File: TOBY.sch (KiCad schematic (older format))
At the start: 36 parts, among them Q301 2N7002BKT, U301 U-BLOX-TOBY-L2, X301 ANT, X302 SIMcard, X303 ANT

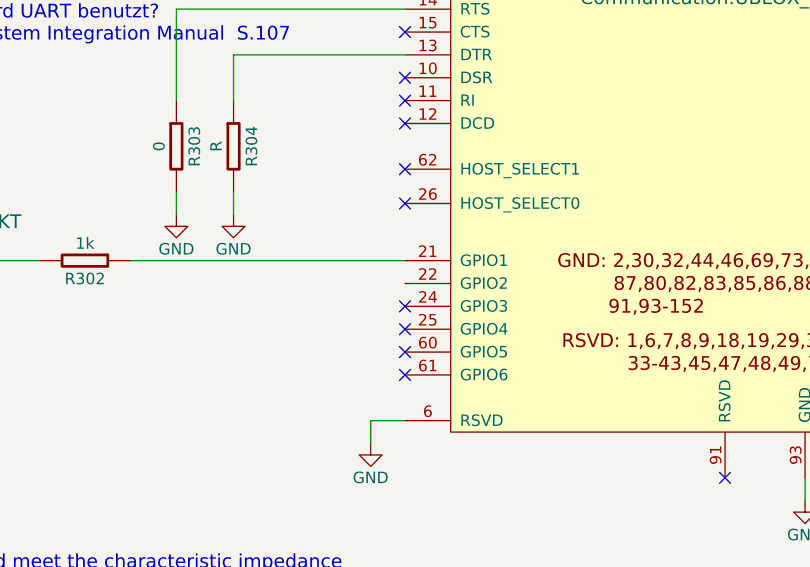
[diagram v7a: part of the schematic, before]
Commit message: adjusted 3d models
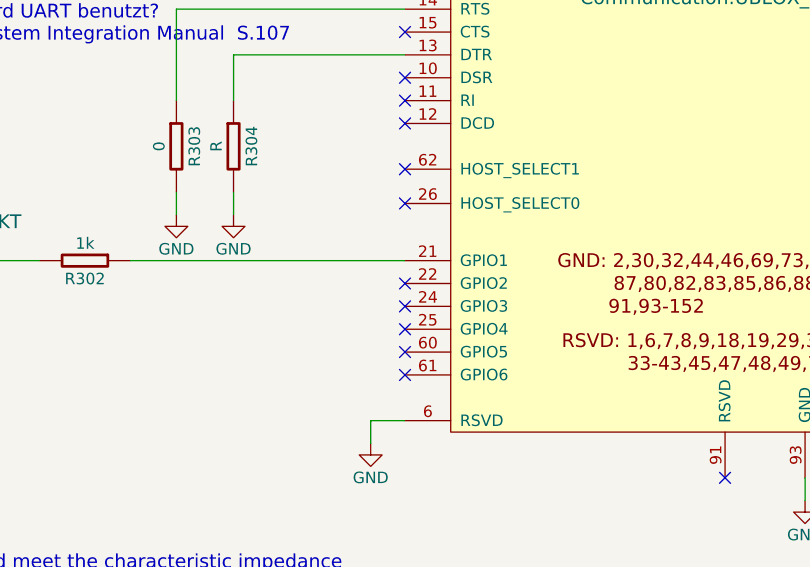
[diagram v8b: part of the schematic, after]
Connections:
- no-connect marks 26 -> 27
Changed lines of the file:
@@
 $EndComp
 $Comp
-L GND #PWR321
+L GND #PWR084
 U 1 1 570E3CB9
 P 9100 2450
-F 0 "#PWR321" H 9100 2200 50  0001 C CNN
+F 0 "#PWR084" H 9100 2200 50  0001 C CNN
 F 1 "GND" H 9100 2300 50  0000 C CNN
 F 2 "" H 9100 2450 50  0000 C CNN
@@
 $EndComp
 $Comp
-L GND #PWR322
+L GND #PWR085
 U 1 1 570E6A84
 P 10000 5500
-F 0 "#PWR322" H 10000 5250 50  0001 C CNN
+F 0 "#PWR085" H 10000 5250 50  0001 C CNN
 F 1 "GND" H 10000 5350 50  0000 C CNN
 F 2 "" H 10000 5500 50  0000 C CNN
@@
 $EndComp
 $Comp
-L GND #PWR319
+L GND #PWR086
 U 1 1 570F627C
 P 8550 5950
-F 0 "#PWR319" H 8550 5700 50  0001 C CNN
+F 0 "#PWR086" H 8550 5700 50  0001 C CNN
 F 1 "GND" H 8550 5800 50  0000 C CNN
 F 2 "" H 8550 5950 50  0000 C CNN
@@
 NoConn ~ 5600 5500
 $Comp
-L GND #PWR309
+L GND #PWR087
 U 1 1 570F7F5B
 P 5950 5600
-F 0 "#PWR309" H 5950 5350 50  0001 C CNN
+F 0 "#PWR087" H 5950 5350 50  0001 C CNN
 F 1 "GND" H 5950 5450 50  0000 C CNN
 F 2 "" H 5950 5600 50  0000 C CNN
@@
 $EndComp
 $Comp
-L GND #PWR308
+L GND #PWR088
 U 1 1 570F7F96
 P 4050 5350
-F 0 "#PWR308" H 4050 5100 50  0001 C CNN
+F 0 "#PWR088" H 4050 5100 50  0001 C CNN
 F 1 "GND" H 4050 5200 50  0000 C CNN
 F 2 "" H 4050 5350 50  0000 C CNN
@@
 $EndComp
 $Comp
-L GND #PWR302
+L GND #PWR089
 U 1 1 570FA2F8
 P 1150 2550
-F 0 "#PWR302" H 1150 2300 50  0001 C CNN
+F 0 "#PWR089" H 1150 2300 50  0001 C CNN
 F 1 "GND" H 1150 2400 50  0000 C CNN
 F 2 "" H 1150 2550 50  0000 C CNN
@@
 $EndComp
 $Comp
-L GND #PWR305
+L GND #PWR090
 U 1 1 570FD240
 P 3000 2850
-F 0 "#PWR305" H 3000 2600 50  0001 C CNN
+F 0 "#PWR090" H 3000 2600 50  0001 C CNN
 F 1 "GND" H 3000 2700 50  0000 C CNN
 F 2 "" H 3000 2850 50  0000 C CNN
@@
 $EndComp
 $Comp
-L GND #PWR318
+L GND #PWR091
 U 1 1 571026BC
 P 8500 2800
-F 0 "#PWR318" H 8500 2550 50  0001 C CNN
+F 0 "#PWR091" H 8500 2550 50  0001 C CNN
 F 1 "GND" H 8500 2650 50  0000 C CNN
 F 2 "" H 8500 2800 50  0000 C CNN
@@
 $EndComp
 $Comp
-L GND #PWR316
+L GND #PWR092
 U 1 1 57102715
 P 8200 2800
-F 0 "#PWR316" H 8200 2550 50  0001 C CNN
+F 0 "#PWR092" H 8200 2550 50  0001 C CNN
 F 1 "GND" H 8200 2650 50  0000 C CNN
 F 2 "" H 8200 2800 50  0000 C CNN
@@
 $EndComp
 $Comp
-L GND #PWR314
+L GND #PWR093
 U 1 1 5710276E
 P 7900 2800
-F 0 "#PWR314" H 7900 2550 50  0001 C CNN
+F 0 "#PWR093" H 7900 2550 50  0001 C CNN
 F 1 "GND" H 7900 2650 50  0000 C CNN
 F 2 "" H 7900 2800 50  0000 C CNN
@@
 $EndComp
 $Comp
-L GND #PWR312
+L GND #PWR094
 U 1 1 571027C7
 P 7600 2800
-F 0 "#PWR312" H 7600 2550 50  0001 C CNN
+F 0 "#PWR094" H 7600 2550 50  0001 C CNN
 F 1 "GND" H 7600 2650 50  0000 C CNN
 F 2 "" H 7600 2800 50  0000 C CNN
@@
 $EndComp
 $Comp
-L GND #PWR320
+L GND #PWR095
 U 1 1 571028B7
 P 8800 2800
-F 0 "#PWR320" H 8800 2550 50  0001 C CNN
+F 0 "#PWR095" H 8800 2550 50  0001 C CNN
 F 1 "GND" H 8800 2650 50  0000 C CNN
 F 2 "" H 8800 2800 50  0000 C CNN
@@
 	2050 4200 2050 4300
 $Comp
-L GND #PWR304
+L GND #PWR096
 U 1 1 57105942
 P 2050 4900
-F 0 "#PWR304" H 2050 4650 50  0001 C CNN
+F 0 "#PWR096" H 2050 4650 50  0001 C CNN
 F 1 "GND" H 2050 4750 50  0000 C CNN
 F 2 "" H 2050 4900 50  0000 C CNN
@@
 $EndComp
 $Comp
-L +3V3 #PWR303
+L +3V3 #PWR097
 U 1 1 57105A00
 P 2050 3200
-F 0 "#PWR303" H 2050 3050 50  0001 C CNN
+F 0 "#PWR097" H 2050 3050 50  0001 C CNN
 F 1 "+3V3" H 2050 3340 50  0000 C CNN
 F 2 "" H 2050 3200 50  0000 C CNN
@@
 	3450 3650 3450 3850
 $Comp
-L GND #PWR306
+L GND #PWR098
 U 1 1 5710A931
 P 3200 4350
-F 0 "#PWR306" H 3200 4100 50  0001 C CNN
+F 0 "#PWR098" H 3200 4100 50  0001 C CNN
 F 1 "GND" H 3200 4200 50  0000 C CNN
 F 2 "" H 3200 4350 50  0000 C CNN
@@
 $EndComp
 $Comp
-L GND #PWR307
+L GND #PWR099
 U 1 1 5710A99F
 P 3450 4350
-F 0 "#PWR307" H 3450 4100 50  0001 C CNN
+F 0 "#PWR099" H 3450 4100 50  0001 C CNN
 F 1 "GND" H 3450 4200 50  0000 C CNN
 F 2 "" H 3450 4350 50  0000 C CNN
@@
 NoConn ~ 7150 3150
 $Comp
-L +3V8 #PWR301
+L +3V8 #PWR0100
 U 1 1 57114B92
 P 1150 1500
-F 0 "#PWR301" H 1150 1350 50  0001 C CNN
+F 0 "#PWR0100" H 1150 1350 50  0001 C CNN
 F 1 "+3V8" H 1150 1640 50  0000 C CNN
 F 2 "" H 1150 1500 50  0000 C CNN
@@
 Connection ~ 4000 1750
 $Comp
-L +1V8 #PWR310
+L +1V8 #PWR0101
 U 1 1 57168AFB
 P 7400 1500
-F 0 "#PWR310" H 7400 1350 50  0001 C CNN
+F 0 "#PWR0101" H 7400 1350 50  0001 C CNN
 F 1 "+1V8" H 7400 1640 50  0000 C CNN
 F 2 "" H 7400 1500 50  0000 C CNN
@@
 	7400 1600 7400 1500
 $Comp
-L GND #PWR323
+L GND #PWR0102
 U 1 1 571D4F40
 P 10600 2500
-F 0 "#PWR323" H 10600 2250 50  0001 C CNN
+F 0 "#PWR0102" H 10600 2250 50  0001 C CNN
 F 1 "GND" H 10600 2350 50  0000 C CNN
 F 2 "" H 10600 2500 50  0000 C CNN
@@
 $EndComp
 $Comp
-L GND #PWR311
+L GND #PWR0103
 U 1 1 5723D09C
 P 7600 1000
-F 0 "#PWR311" H 7600 750 50  0001 C CNN
+F 0 "#PWR0103" H 7600 750 50  0001 C CNN
 F 1 "GND" H 7600 850 50  0000 C CNN
 F 2 "" H 7600 1000 50  0000 C CNN
@@
 $EndComp
 $Comp
-L GND #PWR313
+L GND #PWR0104
 U 1 1 5723D15B
 P 7900 1000
-F 0 "#PWR313" H 7900 750 50  0001 C CNN
+F 0 "#PWR0104" H 7900 750 50  0001 C CNN
 F 1 "GND" H 7900 850 50  0000 C CNN
 F 2 "" H 7900 1000 50  0000 C CNN
@@
 $EndComp
 $Comp
-L GND #PWR315
+L GND #PWR0105
 U 1 1 5723D1D2
 P 8200 1000
-F 0 "#PWR315" H 8200 750 50  0001 C CNN
+F 0 "#PWR0105" H 8200 750 50  0001 C CNN
 F 1 "GND" H 8200 850 50  0000 C CNN
 F 2 "" H 8200 1000 50  0000 C CNN
@@
 $EndComp
 $Comp
-L GND #PWR317
+L GND #PWR0106
 U 1 1 5723D249
 P 8500 1000
-F 0 "#PWR317" H 8500 750 50  0001 C CNN
+F 0 "#PWR0106" H 8500 750 50  0001 C CNN
 F 1 "GND" H 8500 850 50  0000 C CNN
 F 2 "" H 8500 1000 50  0000 C CNN
@@
 Text Notes 2300 3600 0    60   ~ 0
 Wird UART benutzt?\nSystem Integration Manual  S.107
+NoConn ~ 4200 4650
 $EndSCHEMATC
